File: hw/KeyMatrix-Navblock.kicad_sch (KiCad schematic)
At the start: 50 parts, among them SW4300 SW_Cherry_MX_RGB, SW4301 SW_Cherry_MX_RGB, SW4302 SW_Cherry_MX_RGB, SW4303 SW_Cherry_MX_RGB, SW4304 SW_Cherry_MX_RGB, SW4305 SW_Cherry_MX_RGB, SW4306 SW_Cherry_MX_RGB, SW4307 SW_Cherry_MX_RGB, SW4308 SW_Cherry_MX_RGB, SW4309 SW_Cherry_MX_RGB, SW4310 SW_Cherry_MX_RGB, SW4311 SW_Cherry_MX_RGB, SW4312 SW_Cherry_MX_RGB, SW4313 SW_Cherry_MX_RGB, SW4314 SW_Cherry_MX_RGB, X4300 Keycap-R1-1x1, X4301 Keycap-R1-1x1, X4302 Keycap-R1-1x1, X4303 Keycap-R1-1x1, X4304 Keycap-R1-1x1, X4305 Keycap-R1-1x1, X4306 Keycap-R1-1x1, X4307 Keycap-R1-1x1, X4308 Keycap-R1-1x1, X4309 Keycap-R1-1x1, X4310 Keycap-R1-1x1, X4311 Keycap-R1-1x1, X4312 Keycap-R1-1x1, X4313 Keycap-R1-1x1, X4314 Keycap-R1-1x1

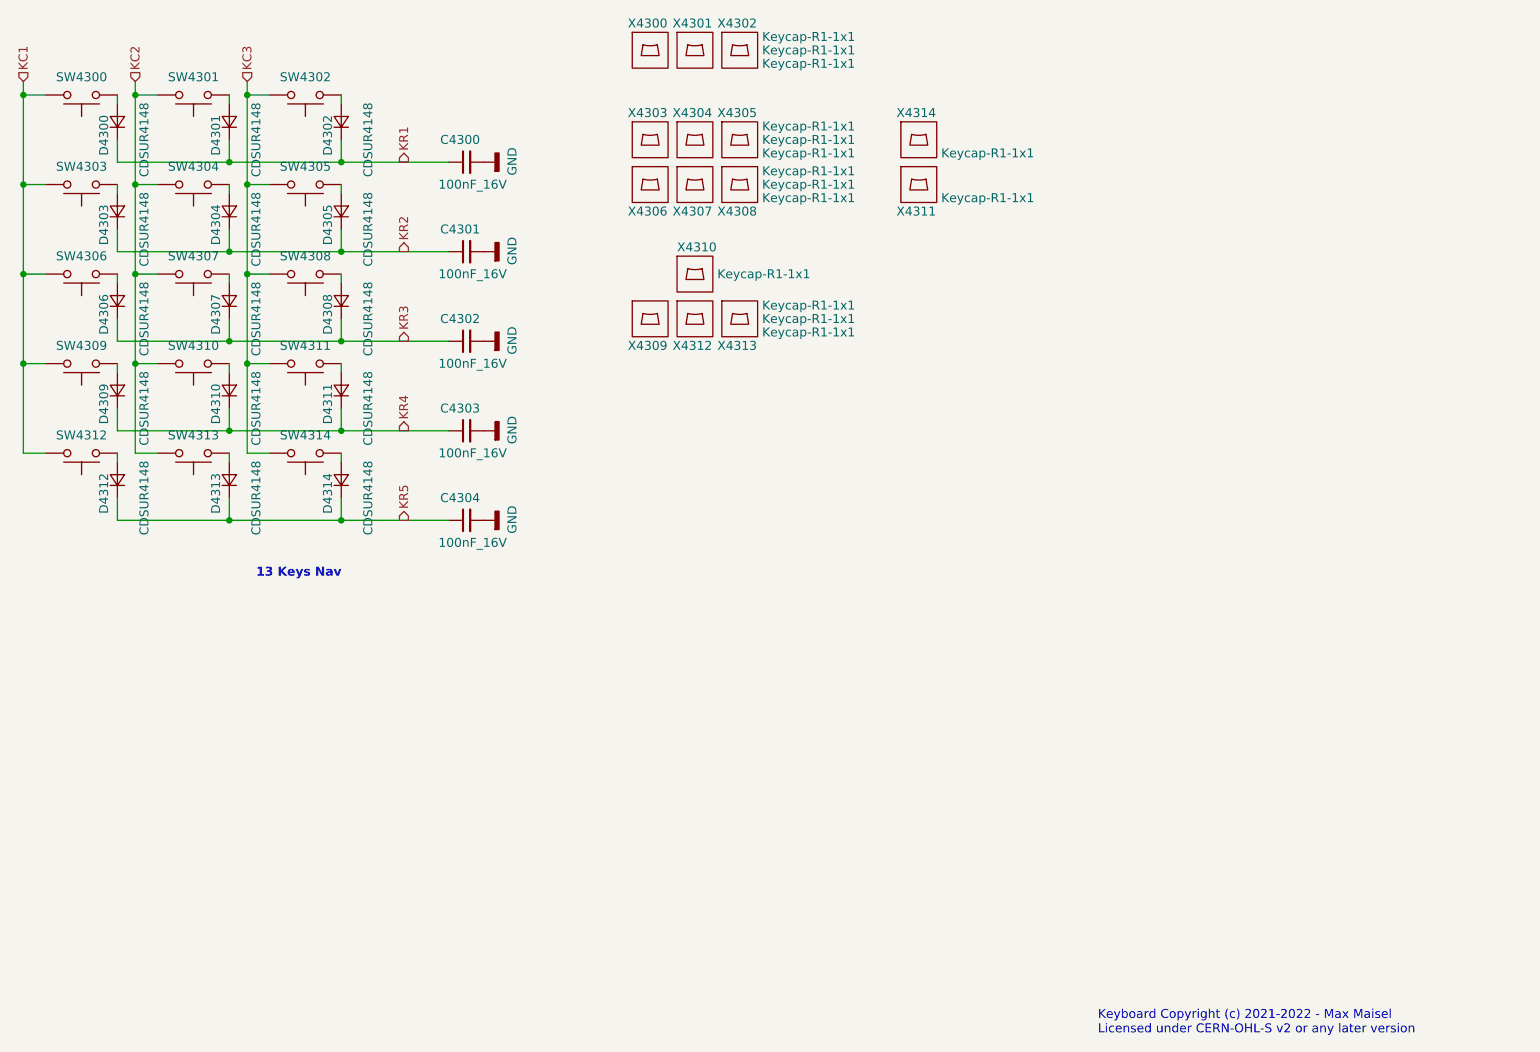
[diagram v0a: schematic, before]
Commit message: Add ESD diodes to key matrix pins.
Better save than sorry.
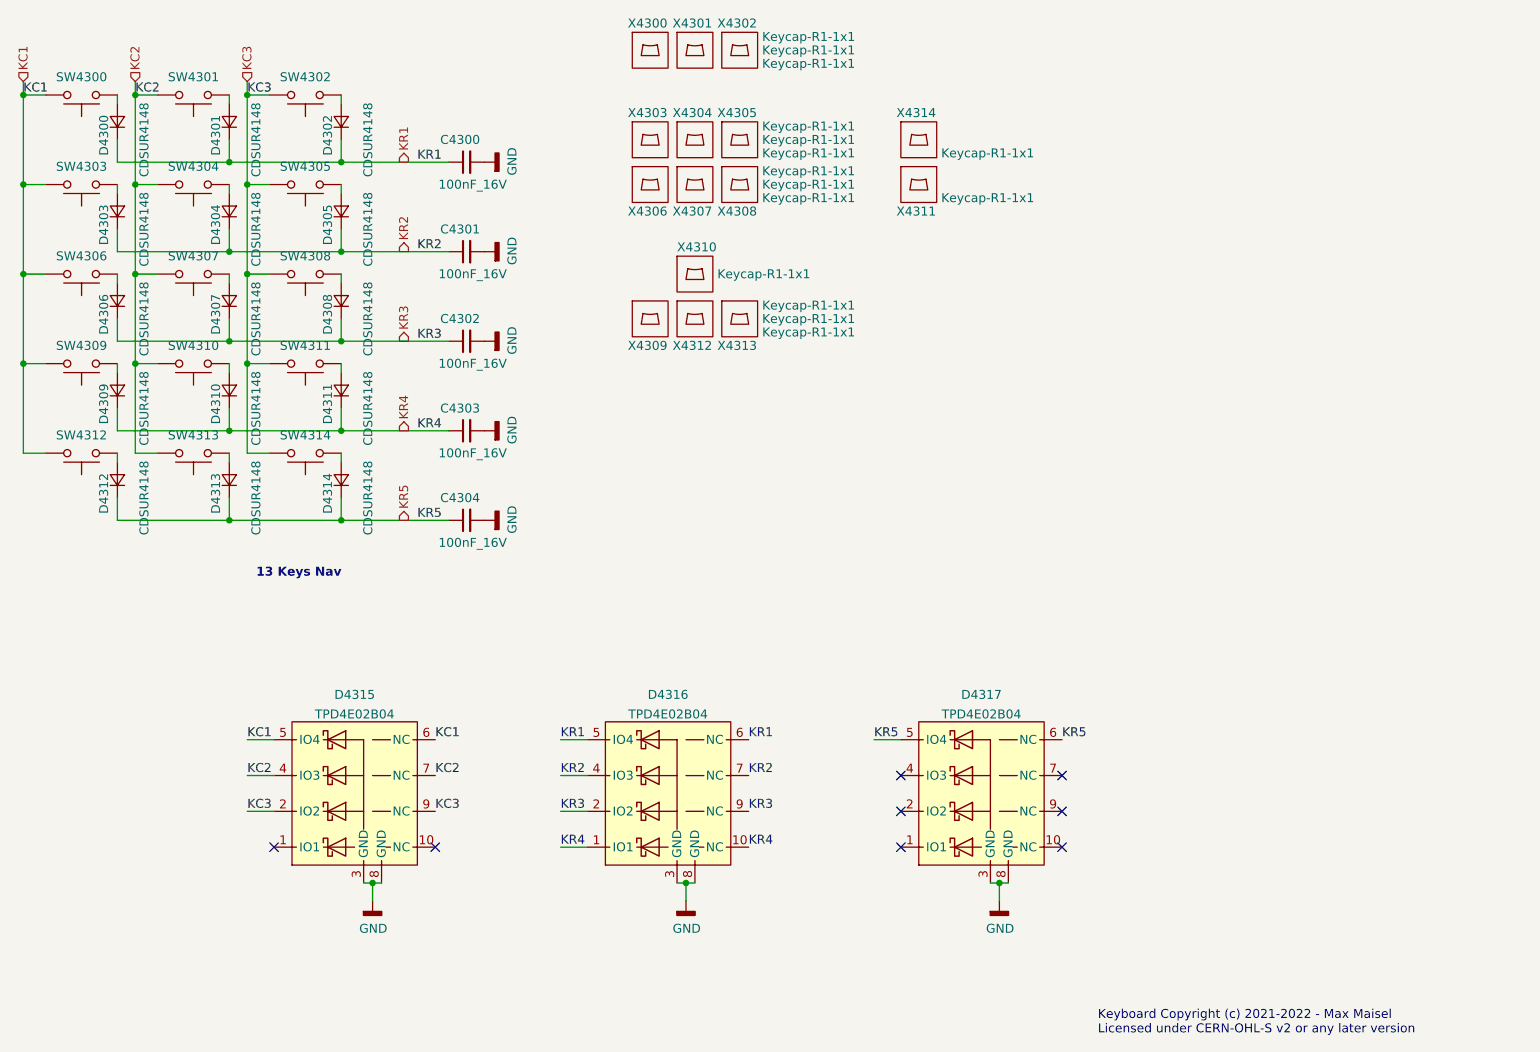
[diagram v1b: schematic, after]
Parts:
- added D4315, D4316, D4317: TPD4E02B04, Keyboard:USON10, symbol Keyboard:TPD4E02B04
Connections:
- net GND: now also D4315.3 (GND), D4315.8 (GND), D4316.3 (GND), D4316.8 (GND), D4317.3 (GND), D4317.8 (GND)
- net KC1: now also D4315.5 (IO4), D4315.6 (NC)
- net KC2: now also D4315.4 (IO3), D4315.7 (NC)
- net KC3: now also D4315.2 (IO2), D4315.9 (NC)
- net KR1: now also D4316.5 (IO4), D4316.6 (NC)
- net KR2: now also D4316.4 (IO3), D4316.7 (NC)
- net KR3: now also D4316.2 (IO2), D4316.9 (NC)
- net KR4: now also D4316.1 (IO1), D4316.10 (NC)
- net KR5: now also D4317.5 (IO4), D4317.6 (NC)
- no-connect marks 0 -> 8

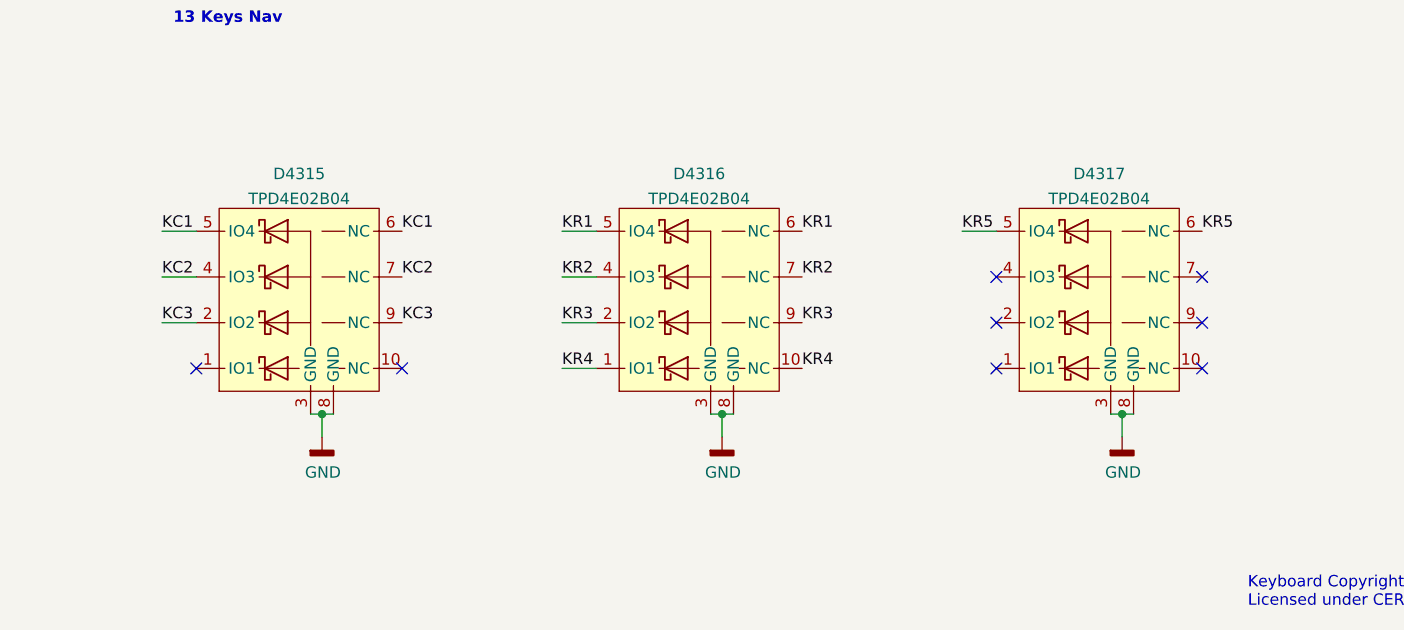
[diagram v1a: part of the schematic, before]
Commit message: Update schematic:
- Add ESD protection.
- Adjust distance bolts so they fit to the MX mounting plate.
- Make key layout symmetric.
- Add resistor to TX driver outputs.
- Use alternate IO functions on inter-board connectors.
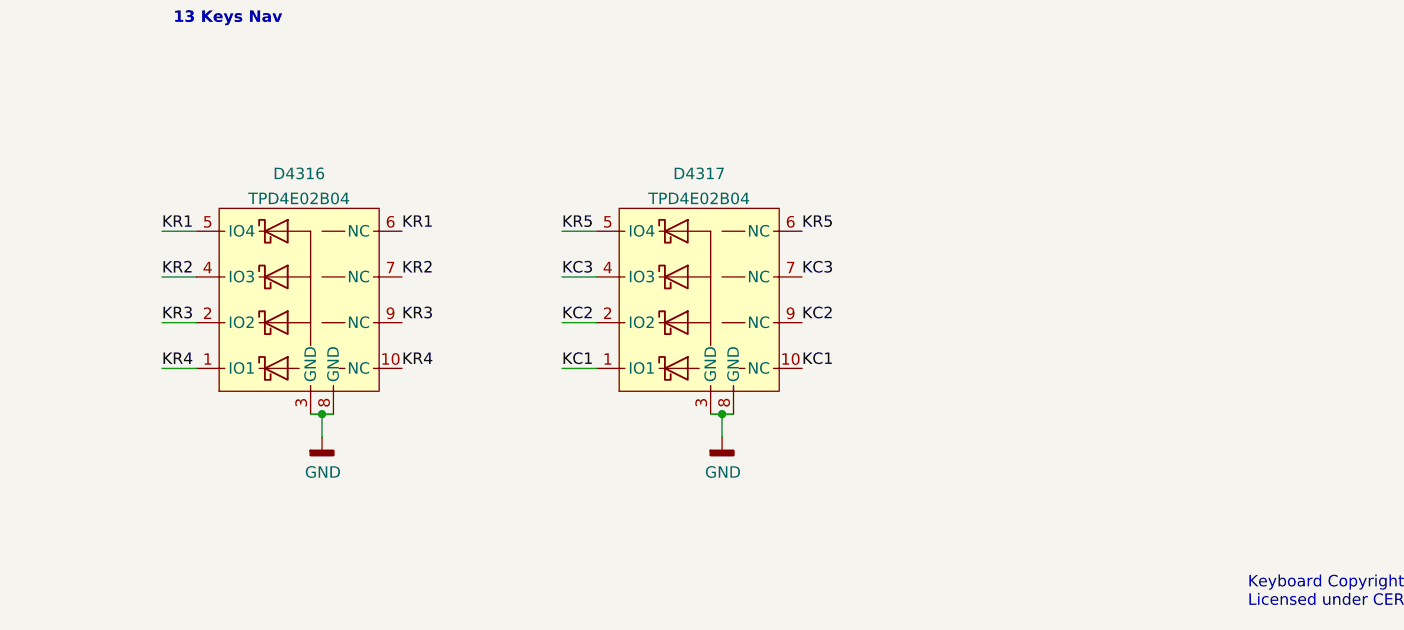
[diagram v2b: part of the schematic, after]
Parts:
- removed D4315: TPD4E02B04, Keyboard:USON10, symbol Keyboard:TPD4E02B04
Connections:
- net KC1: now also D4317.1 (IO1), D4317.10 (NC)
- net KC2: now also D4317.2 (IO2), D4317.9 (NC)
- net KC3: now also D4317.4 (IO3), D4317.7 (NC)
- no-connect marks 8 -> 0
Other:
- moved on the sheet: D4316, D4317
